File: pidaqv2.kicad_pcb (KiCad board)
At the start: 2 copper layers, 26 parts, among them J101 Screw_Terminal_01x10, J102 Screw_Terminal_01x06, J103 Conn_01x02_Male, J104 Screw_Terminal_01x04, J105 Screw_Terminal_01x08, U201 ADS1261BIRHBR, U301 ADS1261BIRHBR, U401 AD8426ACPZ-R7

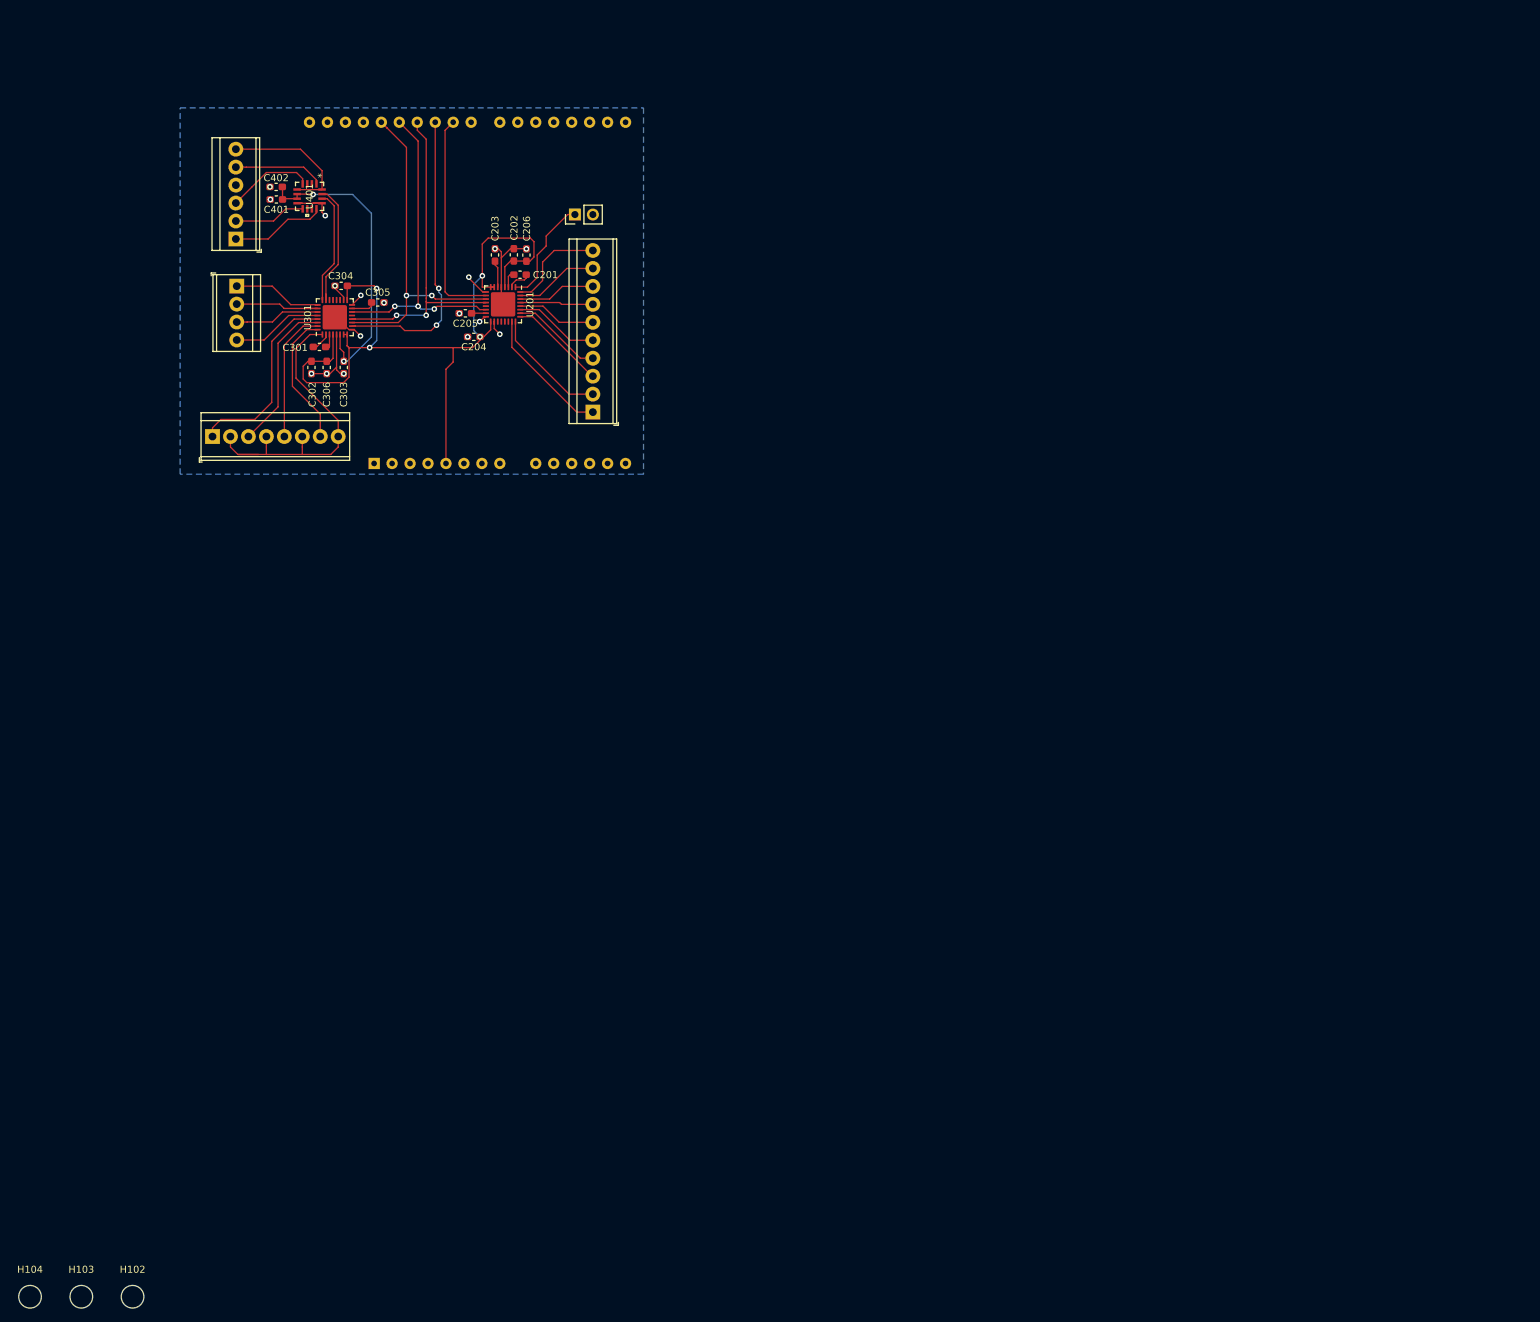
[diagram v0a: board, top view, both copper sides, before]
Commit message: without silkscreen
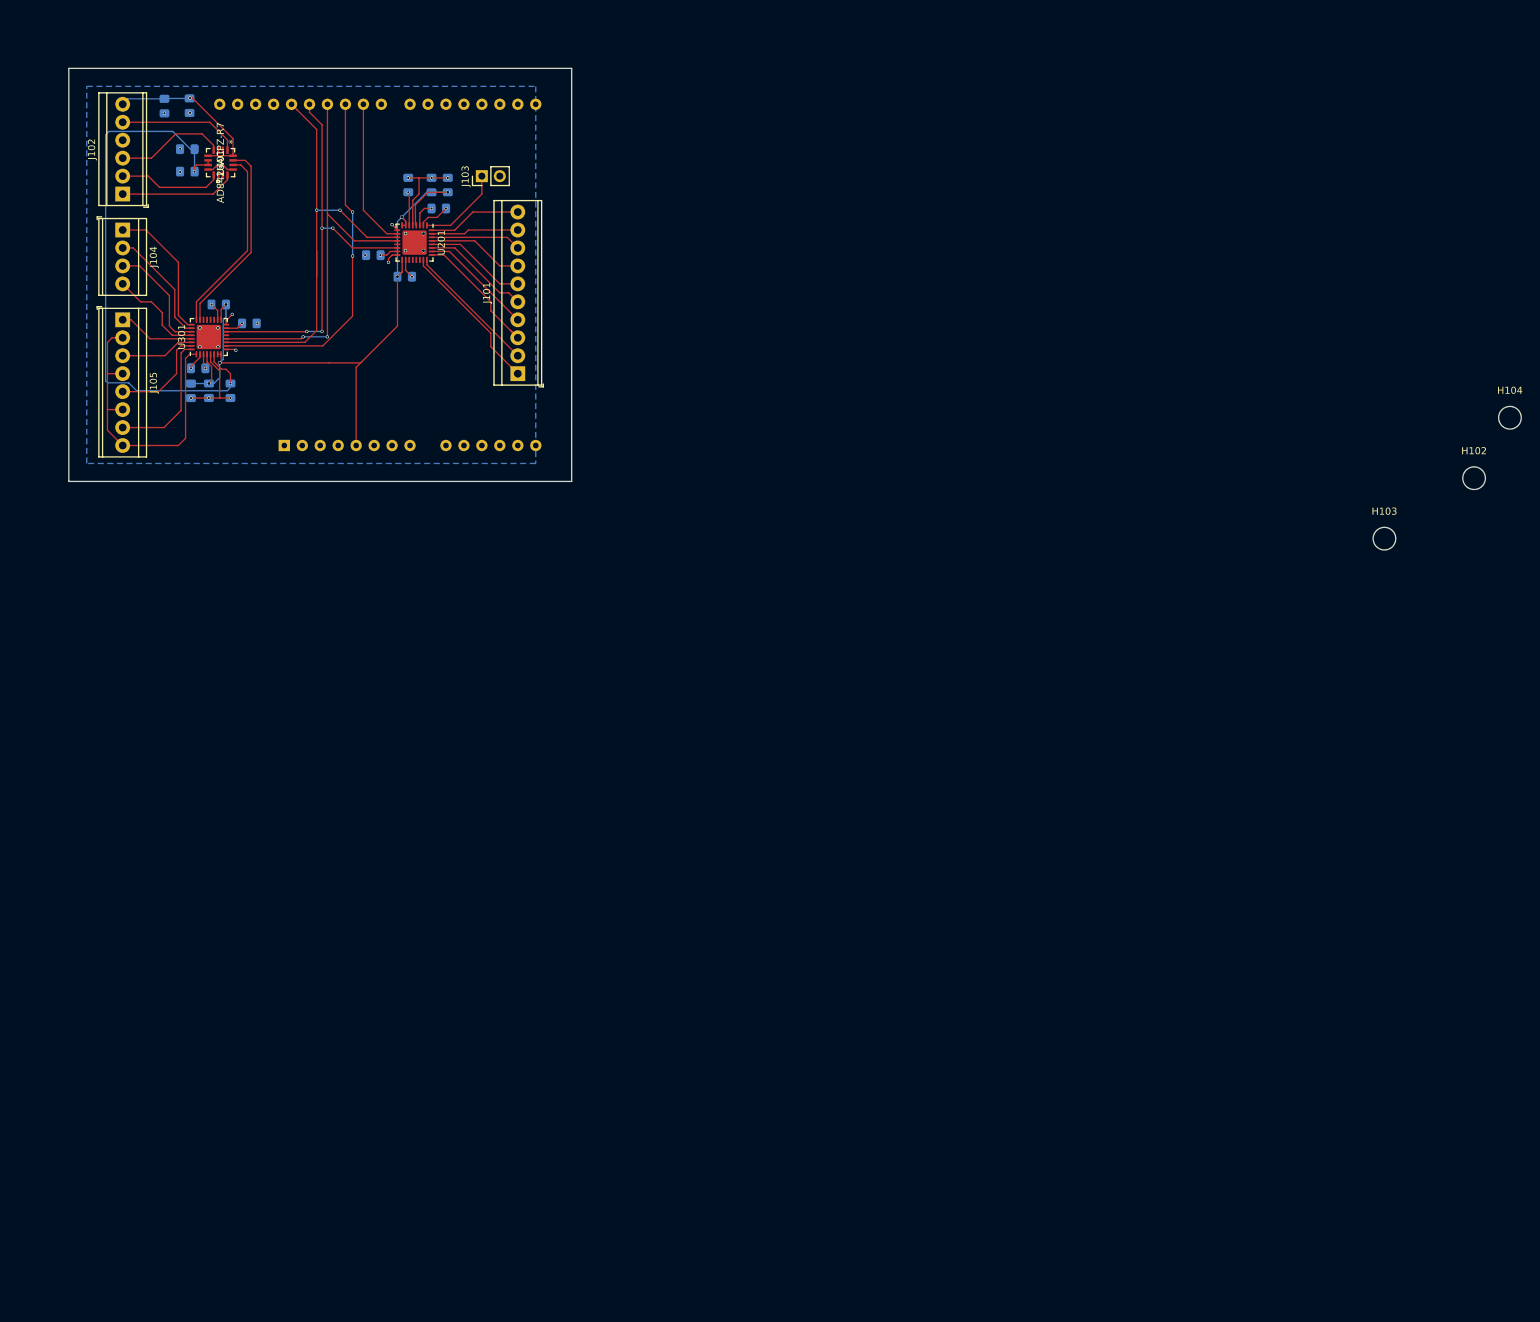
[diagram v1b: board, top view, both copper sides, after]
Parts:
- added C403: 0.1uF, Capacitor_SMD:C_0805_2012Metric_Pad1.15x1.40mm_HandSolder, B.Cu at (117.7, 73.9)
- added C404: 10uF, Capacitor_SMD:C_0805_2012Metric_Pad1.15x1.40mm_HandSolder, B.Cu at (121.2, 73.9)
- C201, C202, C203, C204, C205, C206, C301, C302, C303, C304, C305, C306, C401, C402: footprint Capacitor_SMD:C_0603_1608Metric_Pad1.05x0.95mm_HandSolder -> Capacitor_SMD:C_0805_2012Metric_Pad1.15x1.40mm_HandSolder; moved to B.Cu
- moved H104 243.4 mm to (308.0, 118.0)
- moved H102 222.3 mm to (302.9, 126.5)
- moved H103 213.2 mm to (290.2, 135.1)
- moved J105 20.8 mm to (111.8, 104.1), turned to 270 degrees
- moved C305 18.4 mm to (129.7, 104.6)
- moved U301 18.0 mm to (123.9, 106.6)
- moved J104 18.0 mm to (111.8, 91.4)
- moved C304 17.5 mm to (125.3, 102.0)
- moved C301 17.4 mm to (122.4, 111.0)
- moved C302 17.4 mm to (121.4, 114.2)
- moved J102 17.2 mm to (111.8, 86.4)
- moved C306 17.0 mm to (124.0, 114.2)
- moved C303 16.4 mm to (127.0, 114.2)
- moved C203 15.8 mm to (152.1, 85.1)
- moved C205 15.4 mm to (147.2, 95.0)
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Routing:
- net 2.5V: track 43.0 -> 79.6 mm
- net /ADC1/AIN3: track 27.5 -> 10.9 mm
- net SCLK: track 48.3 -> 63.5 mm
- net +5V: track 114.0 -> 101.9 mm, vias 4 -> 6
- net MISO: track 46.9 -> 58.4 mm, vias 3 -> 4
- net /ADC1/AIN2: track 21.7 -> 10.5 mm
- net MOSI: track 47.8 -> 58.8 mm
- net ~CS0: track 31.1 -> 21.2 mm
- net /B: track 16.6 -> 26.4 mm
- net /A: track 17.9 -> 27.6 mm
- net ~CS1: track 42.2 -> 50.0 mm
- net /ADC1/AIN7: track 12.5 -> 19.7 mm
- net GND: track 46.9 -> 40.6 mm, vias 17 -> 27
- net /ADC0/AIN7: track 13.7 -> 19.2 mm
- net /amplifier/VEXC: track 19.7 -> 24.3 mm, vias 0 -> 1
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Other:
- board outline added: 71.1 x 58.4 mm
- net class Default: clearance 0.1778 -> 0.127; trace_width 0.1778 -> 0.127; via_dia 0.8 -> 0.4572; via_drill 0.4 -> 0.3048
- net class Power: clearance 0.1778 -> 0.127; trace_width 0.508 -> 0.1778; via_dia 0.8 -> 0.508; via_drill 0.4 -> 0.4064
- rule trace_clearance: 0.1778 -> 0.127
- rule trace_min: 0.1524 -> 0.127
- rule via_min_drill: 0.381 -> 0.3048
- rule via_min_size: 0.3302 -> 0.4572

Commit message: set up for reviewers
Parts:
- moved H104 177.3 mm to (134.6, 80.6)
- moved H103 165.1 mm to (125.7, 120.7)
- moved H102 146.6 mm to (156.8, 113.7)
- moved J102 12.7 mm to (111.8, 73.7), turned to 270 degrees
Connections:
- J102 pad 1: /amplifier/B- -> /amplifier/VEXC
- J102 pad 2: /amplifier/B+ -> /amplifier/A-
- J102 pad 3: /amplifier/A+ -> GND
- J102 pad 4: GND -> /amplifier/A+
- J102 pad 5: /amplifier/A- -> /amplifier/B+
- J102 pad 6: /amplifier/VEXC -> /amplifier/B-
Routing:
- net 2.5V: track 79.6 -> 80.8 mm, vias 2 -> 4
- net /amplifier/VEXC: track 24.3 -> 25.4 mm
- net +5V: track 101.9 -> 101.1 mm
- net GND: vias 27 -> 25
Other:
- board size 71.1 x 58.4 mm -> 71.1 x 53.3 mm
- board text added: "A+"
- board text added: "A-"
- board text added: "A0"
- board text added: "A1"
- board text added: "A2"
- board text added: "A3"
- board text added: "A4"
- board text added: "A5"
- board text added: "A6"
- board text added: "A7"
- board text added: "A8"
- board text added: "A9"
- board text added: "B+"
- board text added: "B-"
- board text added: "E4"
- board text added: "E5"
- board text added: "E6"
- board text added: "E7"
- board text added: "EX"
- board text added: "GND"
- board text added: "T0+"
- board text added: "T1+"
- board text added: "T2+"
- board text added: "T3+"
- board text added: "TC-"

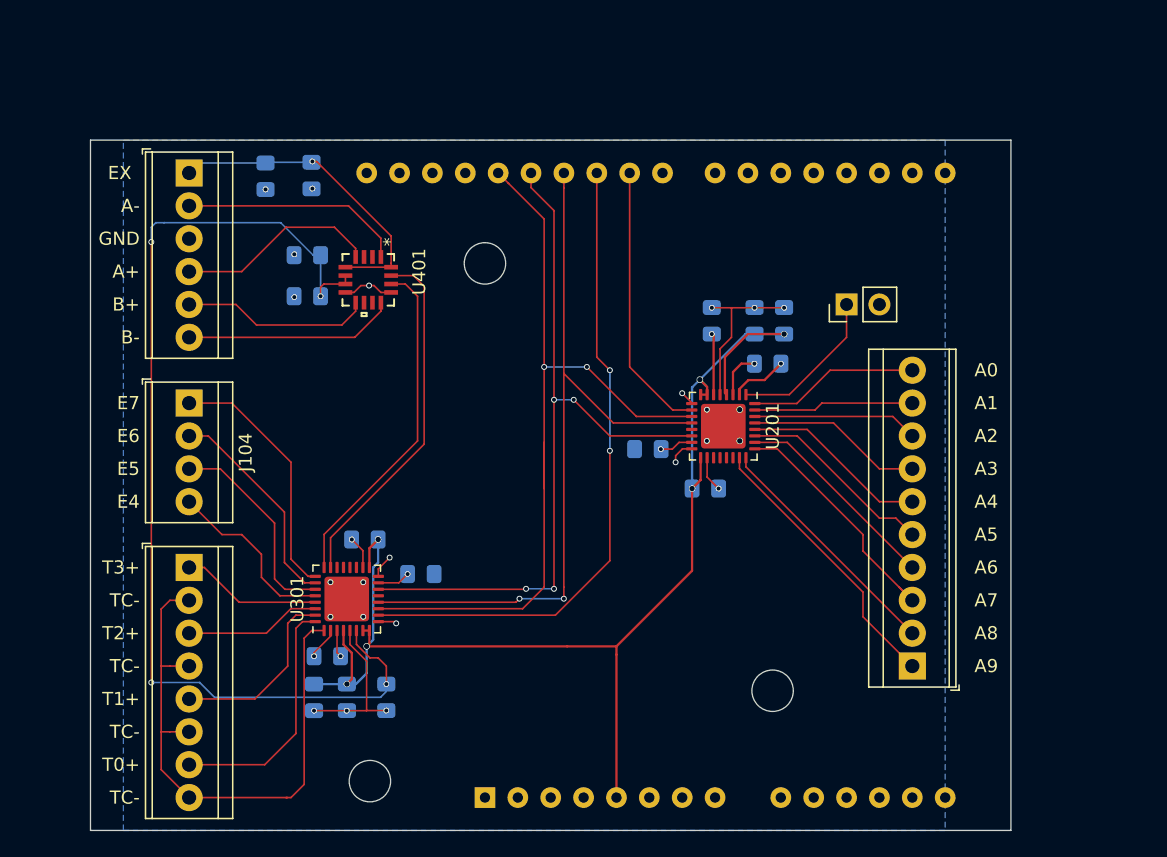
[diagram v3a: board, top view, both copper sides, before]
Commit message: Switched out arduino for raspberry pi
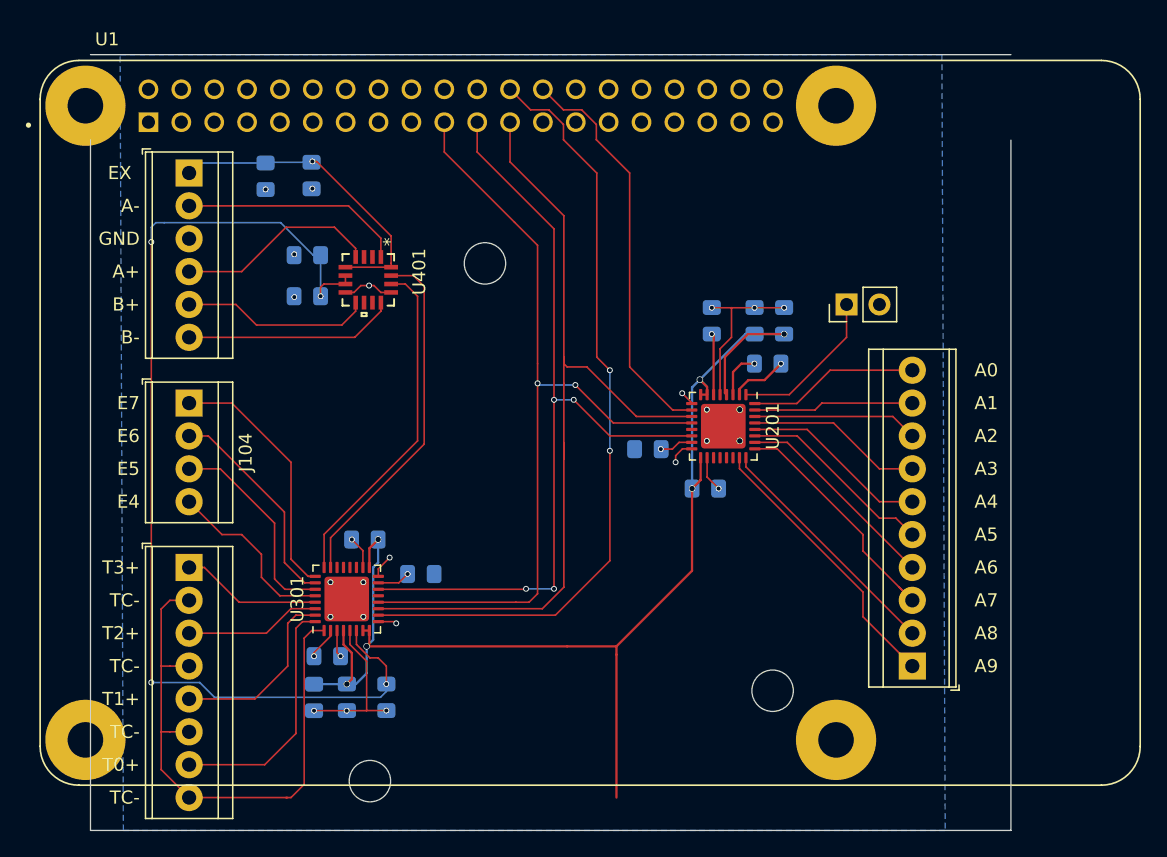
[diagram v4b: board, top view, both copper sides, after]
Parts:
- removed A101: Arduino_UNO_R3, Module:Arduino_UNO_R3
- added U1: RASPBERRY_PI_3_MODEL_B+, RASPBERRY_PI_3_MODEL_B_:MODULE_RASPBERRY_PI_3_MODEL_B+, F.Cu at (142.7, 93.0)
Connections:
- U201 pad 10: ~CS0 -> ~CS1
- U201 pad 13: (no net) -> Net-(U201-Pad13)
- U201 pad 19: (no net) -> Net-(U201-Pad19)
- U201 pad 20: (no net) -> Net-(U201-Pad20)
- U201 pad 21: (no net) -> Net-(U201-Pad21)
- U201 pad 22: (no net) -> Net-(U201-Pad22)
- U301 pad 10: ~CS1 -> ~CS0
- U301 pad 13: (no net) -> Net-(U301-Pad13)
- U301 pad 19: (no net) -> Net-(U301-Pad19)
- U301 pad 20: (no net) -> Net-(U301-Pad20)
- U301 pad 21: (no net) -> Net-(U301-Pad21)
- U301 pad 22: (no net) -> Net-(U301-Pad22)
- U401 pad 10: (no net) -> Net-(U401-Pad10)
- U401 pad 11: (no net) -> Net-(U401-Pad11)
- U401 pad 2: (no net) -> Net-(U401-Pad2)
- U401 pad 3: (no net) -> Net-(U401-Pad3)
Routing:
- net ~CS0: track 21.2 -> 60.1 mm, vias 0 -> 2
- net ~CS1: track 50.0 -> 31.2 mm, vias 2 -> 0
- net MOSI: track 58.8 -> 65.2 mm
- net MISO: track 58.4 -> 64.0 mm
- net SCLK: track 63.5 -> 66.0 mm, vias 2 -> 0
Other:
- board size 71.1 x 53.3 mm -> 71.1 x 59.9 mm
